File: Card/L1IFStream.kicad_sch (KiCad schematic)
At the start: 109 parts, among them J1 Conn_Coaxial, J2 USB_A, J3 RF_Shield_One_Piece, J4 Conn_Coaxial, U1 MAX2769ETI+T, U10 74LVC374, U11 74HC2GU04, U2 TPS717285DCKR, U3 TPS717285DCKR, U4 NCP164CSN330T1G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

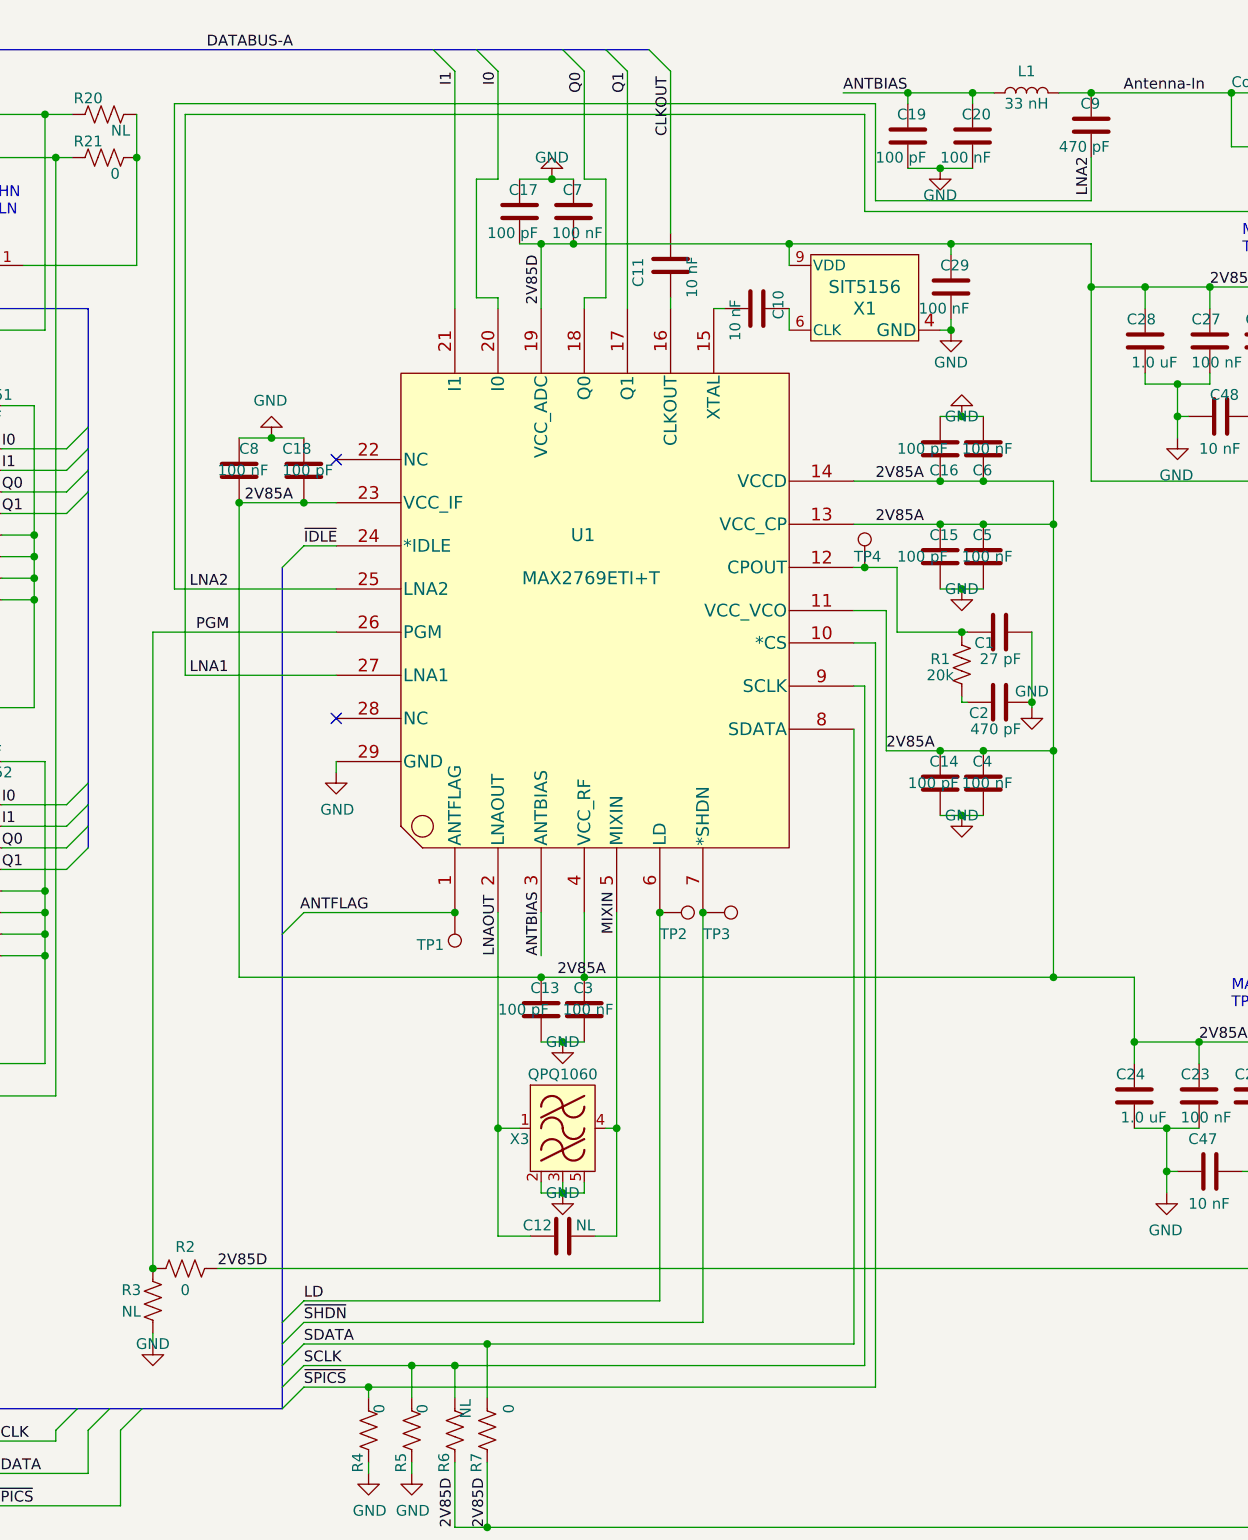
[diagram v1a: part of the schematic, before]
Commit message: Started cleaning up symbol library
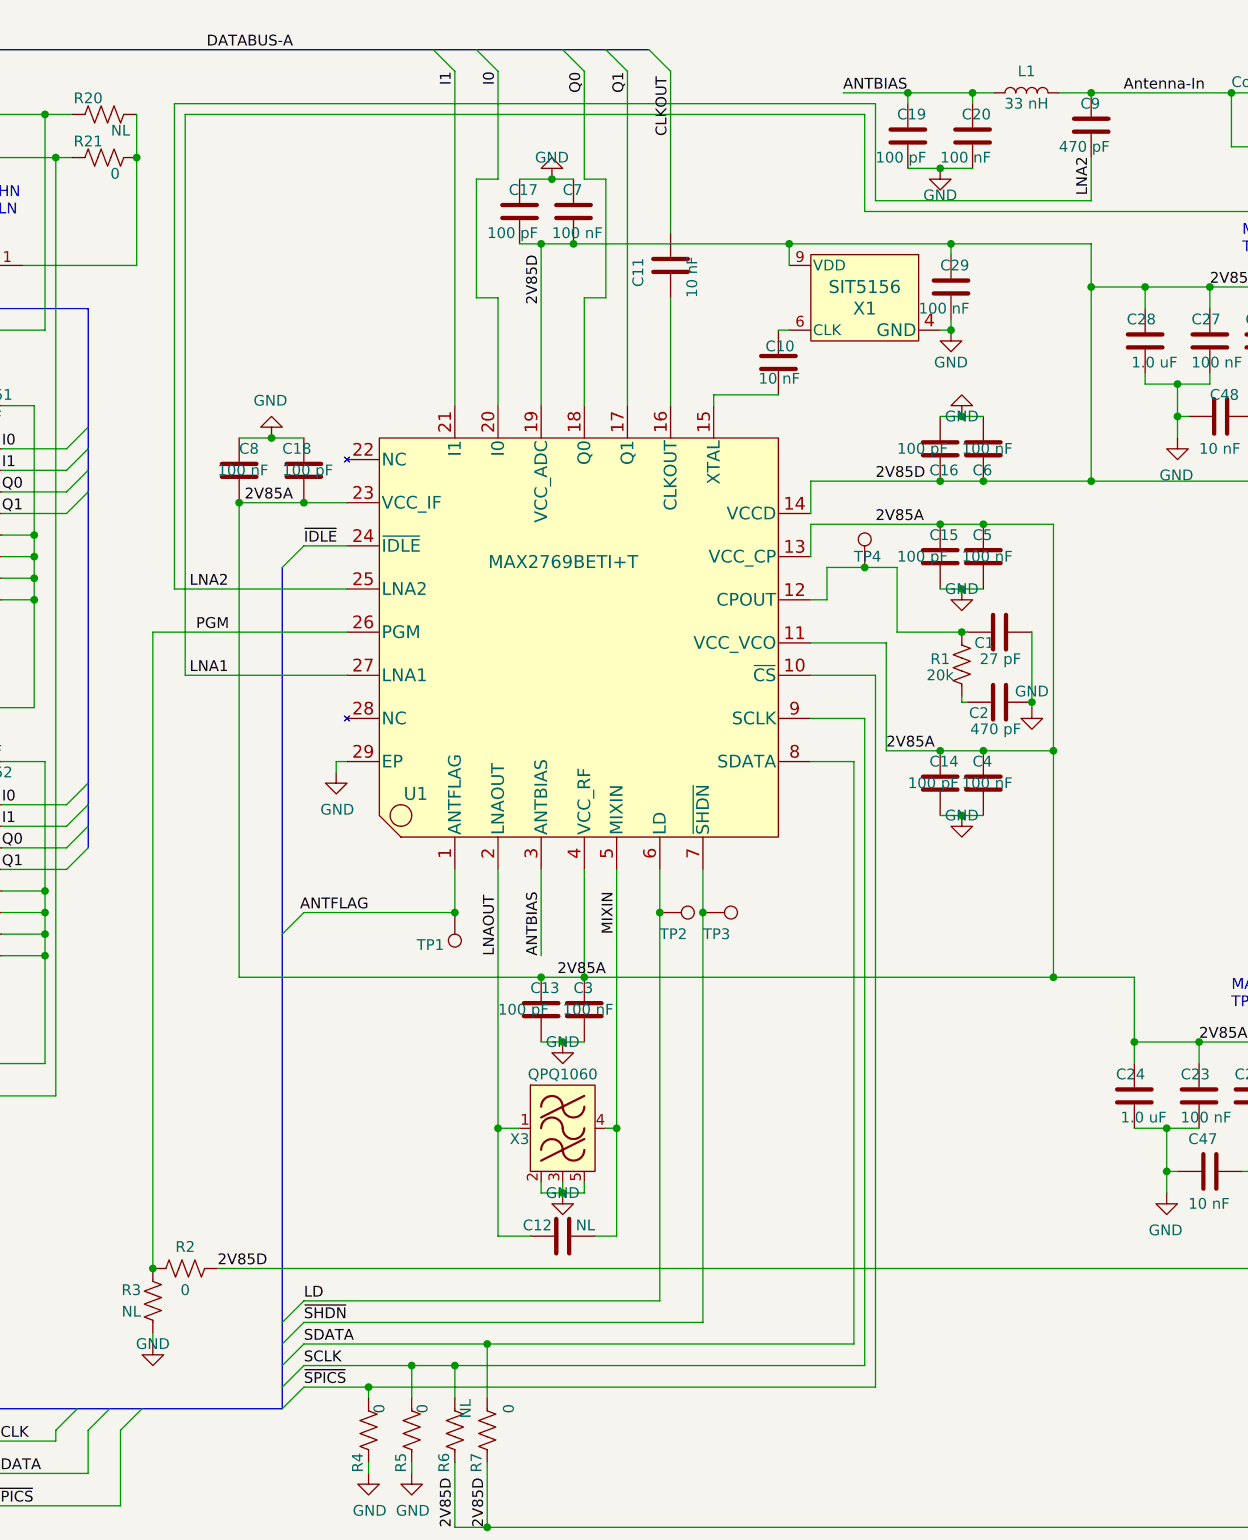
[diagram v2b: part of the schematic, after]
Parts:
- U1: value MAX2769ETI+T -> MAX2769BETI+T; footprint L1IFStream:MAX2769ETI&plus_T -> L1IF:QFN-28_EP_5.63x5.63_Pitch0.5mm; symbol L1IFStream-rescue:MAX2769ETI+T-MAX2769FT2232H -> L1IF:MAX2769ETI+T
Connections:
- net 2V85A: no longer C16.1, C6.1, U1.14 (VCCD)
- net 2V85D: now also C16.1, C6.1, U1.14 (VCCD)
- no-connect marks 26 -> 24
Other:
- moved on the sheet: C10

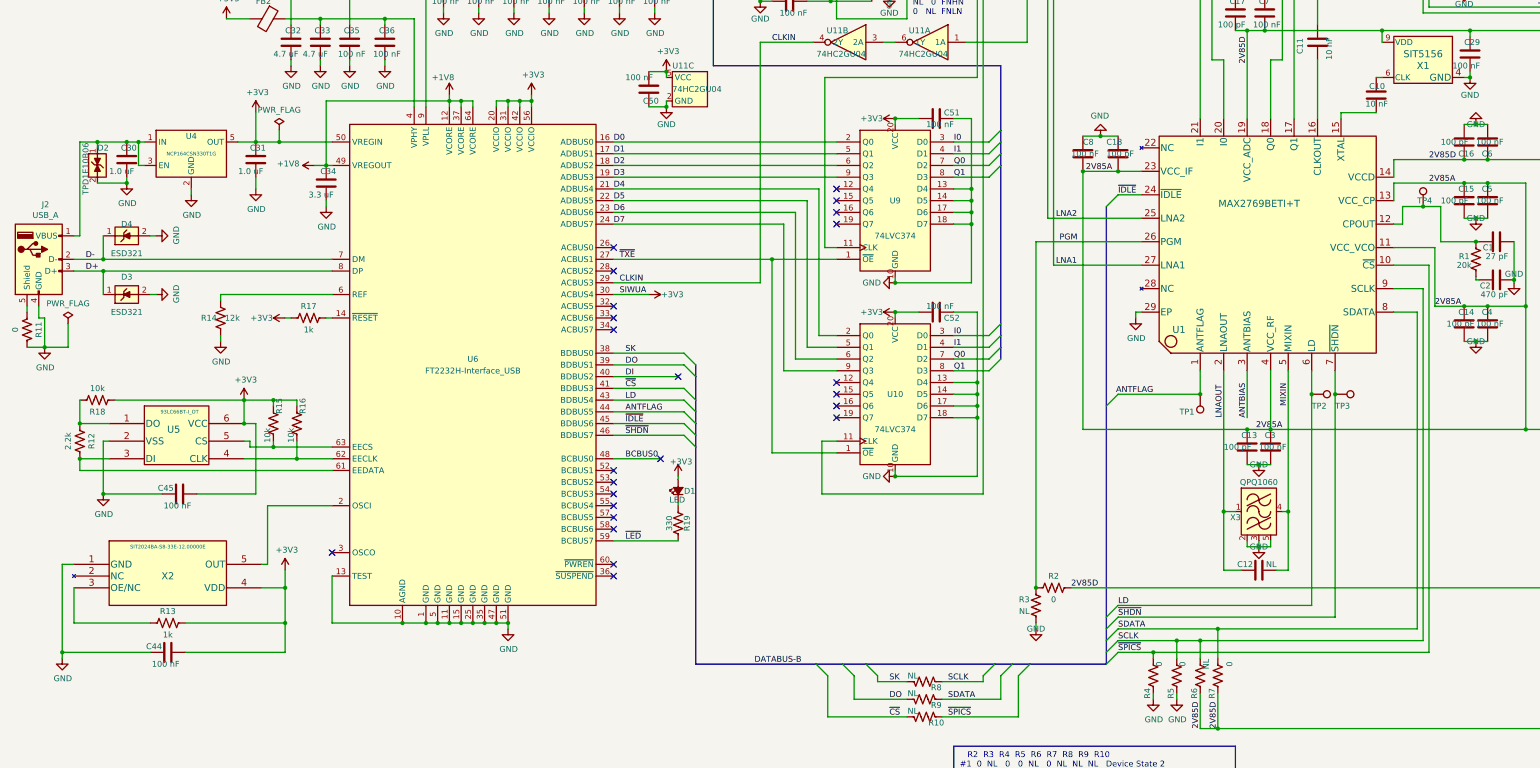
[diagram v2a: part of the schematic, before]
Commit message: Library clean up of oscillators and U1
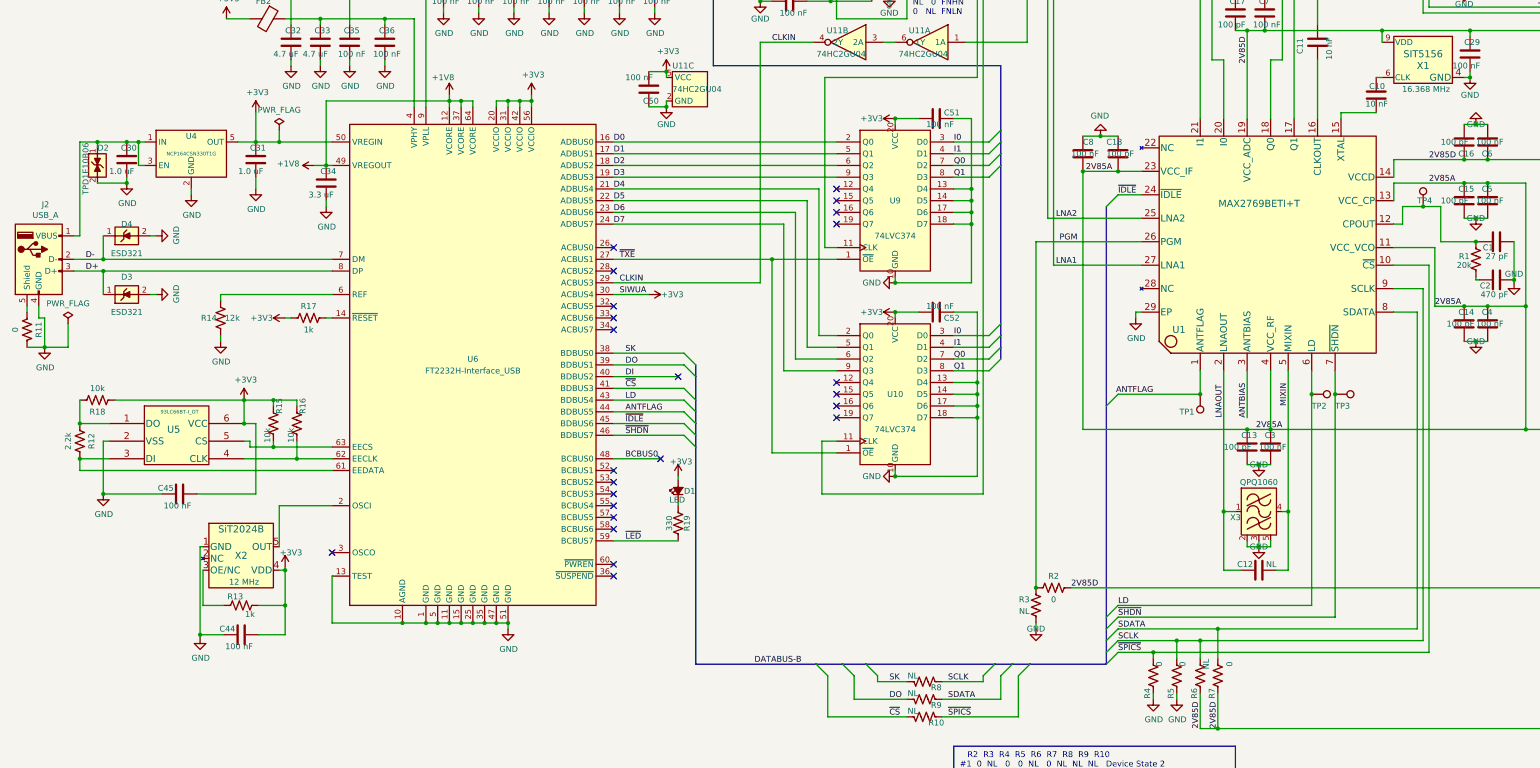
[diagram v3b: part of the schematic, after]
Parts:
- removed X2: SIT2024BA-S8-33E-12.00000E, L1IFStream:SIT2024BA-S8-33E-12.000000E, symbol L1IFStream-rescue:SIT2024BA-S8-33E-12.00000E-MAX2769FT2232H
- added X2: SiT2024B, L1IF:SOT-23-5, symbol L1IF:SIT2024BA-S8-33E-12.00000E
- U1: symbol L1IF:MAX2769ETI+T -> L1IF:MAX2769BETI+T; Vendor P/N# 175-MAX2769BETI/V+-ND -> (none); Vendor PN (none) -> 175-MAX2769BETI/V+-ND
- X1: footprint L1IFStream:10L_CQFN -> L1IF:10L_CQFN; symbol L1IFStream:SIT5156AICFA-30N0-16.368000_1 -> L1IF:SIT5156AICFA-30N0-16.368000_1; Notes (none) -> 16.368 MHz; Vendor P/N# 1473-SIT5156AICFK-30N0-16.368000-ND -> (none); Vendor PN (none) -> 1473-SIT5156AICFK-30N0-16.368000-ND
- X3: footprint L1IFStream:QPQ1060_1.4x1.2 -> L1IF:QPQ1060_1.4x1.2; symbol L1IFStream:QPQ1060 -> L1IF:QPQ1060; Vendor P/N# 772-QPQ1060SR -> (none); Vendor PN (none) -> 772-QPQ1060SR
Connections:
- net +3V3: now also X2.4 (VDD)
- net GND: now also X2.1 (GND)
- net at R13.2: now also X2.3 (OE/NC)
- net at U6.2 (OSCI): now also X2.5 (OUT)
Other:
- moved on the sheet: C44, R13

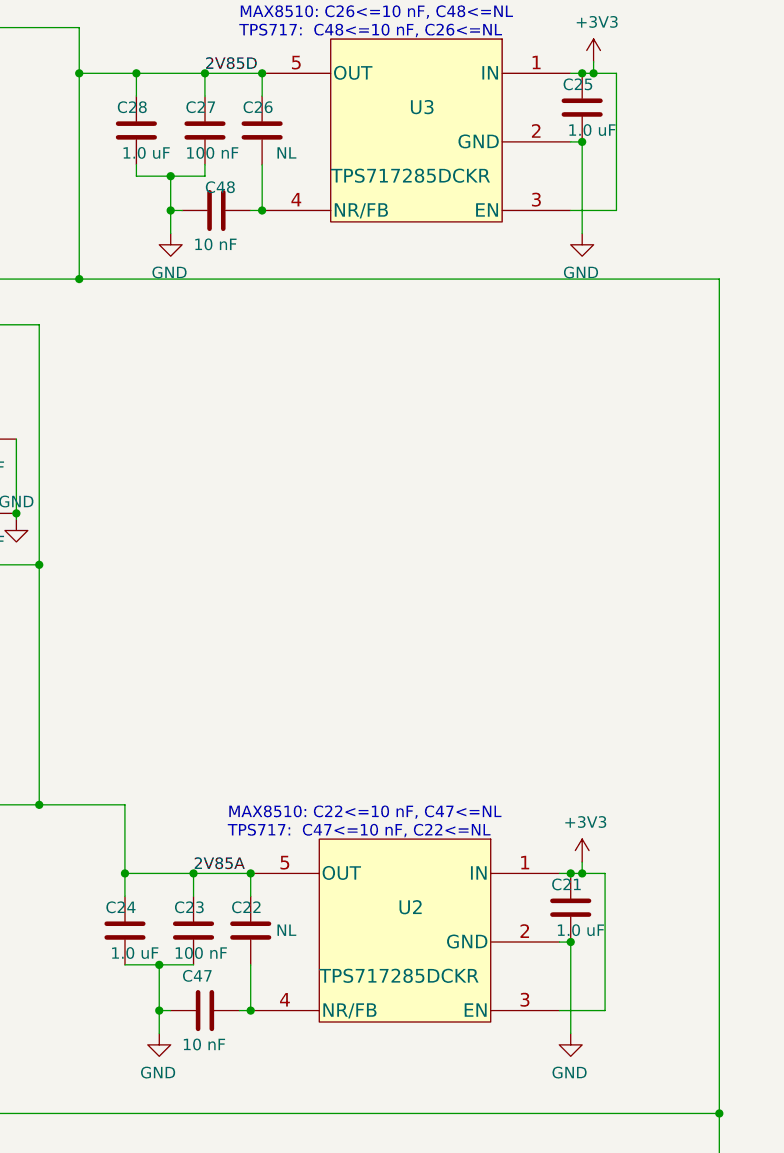
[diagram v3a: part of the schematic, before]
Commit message: Cleaned up library through U3
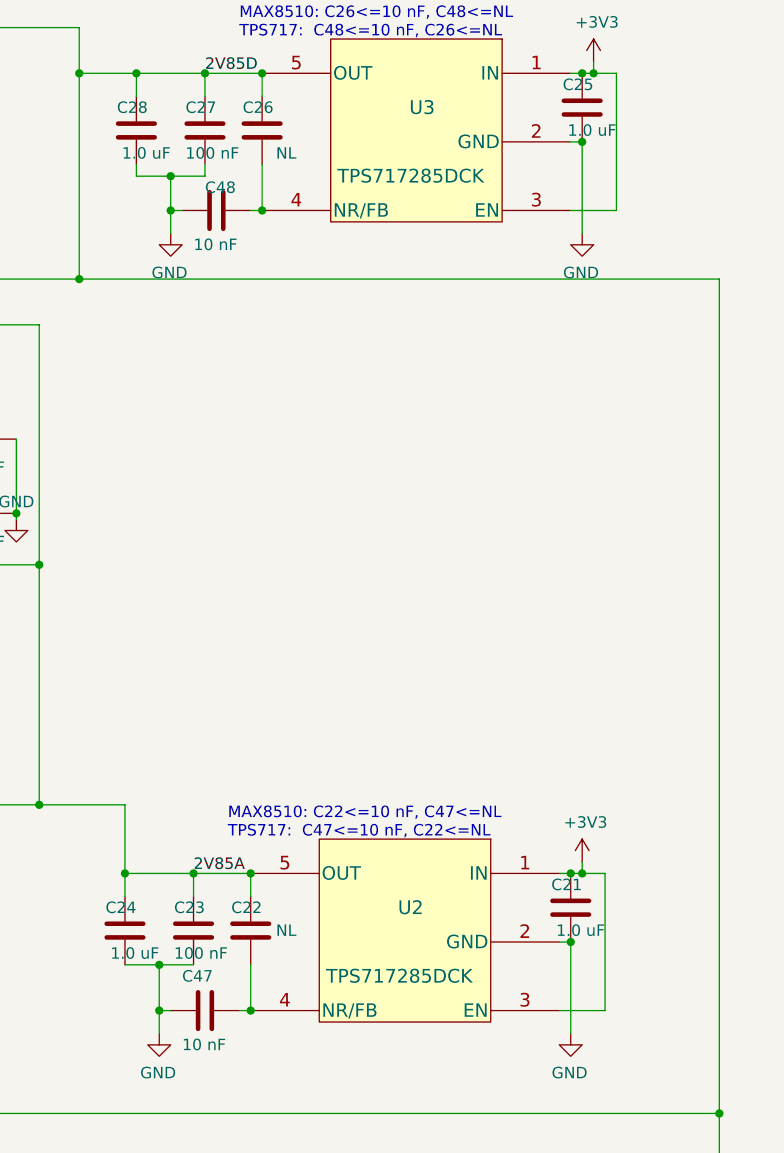
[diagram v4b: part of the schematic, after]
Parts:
- U2, U3: value TPS717285DCKR -> TPS717285DCK; footprint L1IFStream:TPS717285DCKR -> L1IF:TPS717285DCK; symbol L1IFStream-rescue:TPS717285DCKR-MAX2769FT2232H -> L1IF:TPS717285DCK; MPN TPS717285DCKR -> TPS717285DCK; Vendor P/N# 296-19649-1-ND -> (none); Vendor PN (none) -> 296-32541-6-ND
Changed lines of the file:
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@@
     )
   )
-  (symbol (lib_name "TPS717285DCKR-MAX2769FT2232H_1") (lib_id "L1IFStream-rescue:TPS717285DCKR-MAX2769FT2232H") (at 400.05 133.35 0) (mirror y) (unit 1)
+  (symbol (lib_id "L1IF:TPS717285DCK") (at 400.05 133.35 0) (mirror y) (unit 1)
     (in_bom yes) (on_board yes) (dnp no)
     (property "Reference" "U2" (at 383.54 135.89 0)
       (effects (font (size 1.524 1.524)))
     )
-    (property "Value" "TPS717285DCKR" (at 382.27 143.51 0)
+    (property "Value" "TPS717285DCK" (at 382.27 143.51 0)
       (effects (font (size 1.524 1.524)))
     )
-    (property "Footprint" "L1IFStream:TPS717285DCKR" (at 383.54 129.54 0)
+    (property "Footprint" "L1IF:TPS717285DCK" (at 383.54 125.73 0)
       (effects (font (size 1.524 1.524)) hide)
     )
-    (property "Datasheet" "https://www.ti.com/lit/ds/symlink/tps717.pdf" (at 400.05 133.35 0)
+    (property "Datasheet" "https://www.ti.com/lit/ds/symlink/tps717.pdf" (at 386.08 118.11 0)
       (effects (font (size 1.524 1.524)) hide)
     )
-    (property "Description" "IC REG LINEAR 2.85V 150MA SC70-5" (at 400.05 133.35 0)
+    (property "Description" "IC REG LINEAR 2.85V 150MA SC70-5" (at 382.27 123.19 0)
+      (effects (font (size 1.27 1.27)) hide)
+    )
+    (property "Manufacturer" "Texas Instruments" (at 383.54 115.57 0)
+      (effects (font (size 1.27 1.27)) hide)
+    )
+    (property "MPN" "TPS717285DCK" (at 383.54 113.03 0)
       (effects (font (size 1.27 1.27)) hide)
     )
@@
       (effects (font (size 1.27 1.27)) hide)
     )
-    (property "Vendor P/N#" "296-19649-1-ND" (at 400.05 133.35 0)
-      (effects (font (size 1.27 1.27)) hide)
-    )
-    (property "MPN" "TPS717285DCKR" (at 400.05 133.35 0)
-      (effects (font (size 1.27 1.27)) hide)
-    )
-    (property "Manufacturer" "Texas Instruments" (at 400.05 133.35 0)
+    (property "Vendor PN" "296-32541-6-ND" (at 383.54 120.65 0)
       (effects (font (size 1.27 1.27)) hide)
     )
@@
     )
   )
-  (symbol (lib_name "TPS717285DCKR-MAX2769FT2232H_1") (lib_id "L1IFStream-rescue:TPS717285DCKR-MAX2769FT2232H") (at 401.32 44.45 0) (mirror y) (unit 1)
+  (symbol (lib_id "L1IF:TPS717285DCK") (at 401.32 44.45 0) (mirror y) (unit 1)
     (in_bom yes) (on_board yes) (dnp no)
     (property "Reference" "U3" (at 384.81 46.99 0)
       (effects (font (size 1.524 1.524)))
     )
-    (property "Value" "TPS717285DCKR" (at 383.54 54.61 0)
+    (property "Value" "TPS717285DCK" (at 383.54 54.61 0)
       (effects (font (size 1.524 1.524)))
     )
-    (property "Footprint" "L1IFStream:TPS717285DCKR" (at 384.81 40.64 0)
+    (property "Footprint" "L1IF:TPS717285DCK" (at 384.81 36.83 0)
       (effects (font (size 1.524 1.524)) hide)
     )
-    (property "Datasheet" "https://www.ti.com/lit/ds/symlink/tps717.pdf" (at 401.32 44.45 0)
+    (property "Datasheet" "https://www.ti.com/lit/ds/symlink/tps717.pdf" (at 387.35 29.21 0)
       (effects (font (size 1.524 1.524)) hide)
     )
-    (property "Description" "IC REG LINEAR 2.85V 150MA SC70-5" (at 401.32 44.45 0)
+    (property "Description" "IC REG LINEAR 2.85V 150MA SC70-5" (at 383.54 34.29 0)
+      (effects (font (size 1.27 1.27)) hide)
+    )
+    (property "Manufacturer" "Texas Instruments" (at 384.81 26.67 0)
+      (effects (font (size 1.27 1.27)) hide)
+    )
+    (property "MPN" "TPS717285DCK" (at 384.81 24.13 0)
       (effects (font (size 1.27 1.27)) hide)
     )
@@
       (effects (font (size 1.27 1.27)) hide)
     )
-    (property "Vendor P/N#" "296-19649-1-ND" (at 401.32 44.45 0)
-      (effects (font (size 1.27 1.27)) hide)
-    )
-    (property "MPN" "TPS717285DCKR" (at 401.32 44.45 0)
-      (effects (font (size 1.27 1.27)) hide)
-    )
-    (property "Manufacturer" "Texas Instruments" (at 401.32 44.45 0)
-      (effects (font (size 1.27 1.27)) hide)
-    )
+    (property "Vendor PN" "296-32541-6-ND" (at 384.81 31.75 0)
+      (effects (font (size 1.27 1.27)) hide)
+    )
